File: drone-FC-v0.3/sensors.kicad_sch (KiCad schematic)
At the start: 0 parts

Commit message: what
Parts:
- added C11, C13: 0.1uF, Capacitor_SMD:C_0603_1608Metric_Pad1.08x0.95mm_HandSolder, symbol ICM-eagle-import:CAP_CERAMIC0603_NO
- added C12: 4.7uF, Capacitor_SMD:C_0603_1608Metric, symbol Device:C
- added C14, C16, C17: 0.1uF, Capacitor_SMD:C_0603_1608Metric, symbol ICM-eagle-import:CAP_CERAMIC0603_NO
- added C15: 1uF, Capacitor_SMD:C_0603_1608Metric, symbol Device:C
- added J7: ICM, Connector_PinHeader_2.54mm:PinHeader_1x06_P2.54mm_Vertical, symbol Connector:Conn_01x06_Pin
- added J8: UART0, Connector_PinHeader_2.54mm:PinHeader_1x04_P2.54mm_Vertical, symbol Connector:Conn_01x04_Pin
- added R1, R2, R3, R4: 4.7k, Resistor_SMD:R_0603_1608Metric, symbol Device:R
- added U3: LSM6DSOX, Package_LGA:LGA-14_3x2.5mm_P0.5mm_LayoutBorder3x4y, symbol Sensor_Motion:LSM6DSM
- added U4: MS5607-02BA, Package_LGA:LGA-8_3x5mm_P1.25mm, symbol Sensor_Pressure:MS5607-02BA
- added U5: LIS3MDL, Package_LGA:LGA-12_2x2mm_P0.5mm, symbol Sensor_Magnetic:LIS3MDL
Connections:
- new net: C16.1, U5.4 (C1)
- new net +3V3: C11.1, C12.1, C13.1, C14.1, C15.1, C17.1, J7.6 (Pin_6), R1.1, R2.1, R3.1, R4.1, U3.12 (CS), U3.5 (VDDIO), U3.8 (VDD), U4.1 (VDD), U4.2 (PS), U4.4 (CSB), U4.5 (CSB), U4.6 (SDO), U5.10 (~{CS}), U5.5 (Vdd), U5.6 (Vdd_IO)
- new net +5V: J8.3 (Pin_3)
- new net GND: C11.2, C12.2, C13.2, C14.2, C15.2, C16.2, C17.2, J7.4 (Pin_4), J8.4 (Pin_4), U3.1 (SDO/SA0), U3.6 (GND), U3.7 (GND), U4.3 (GND), U5.12 (GND), U5.2 (GND), U5.3 (GND), U5.9 (SDO/SA1)
- new net GPIO11: R3.2, U5.1 (SCL/SPC)
- new net GPIO12: R4.2, U5.11 (SDA/SDI/SDO)
- new net GPIO14: J7.3 (Pin_3)
- new net GPIO16: J7.2 (Pin_2)
- new net RX0: J8.2 (Pin_2)
- new net SCL: R1.2, U3.13 (SCL), U4.8 (SCLK)
- new net SDA: R2.2, U3.14 (SDA), U4.7 (SDI/SDA)
- new net TX0: J8.1 (Pin_1)
- no-connect marks 0 -> 10
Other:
- note added: "Auxiliary Ports"
- note added: "Barometer"

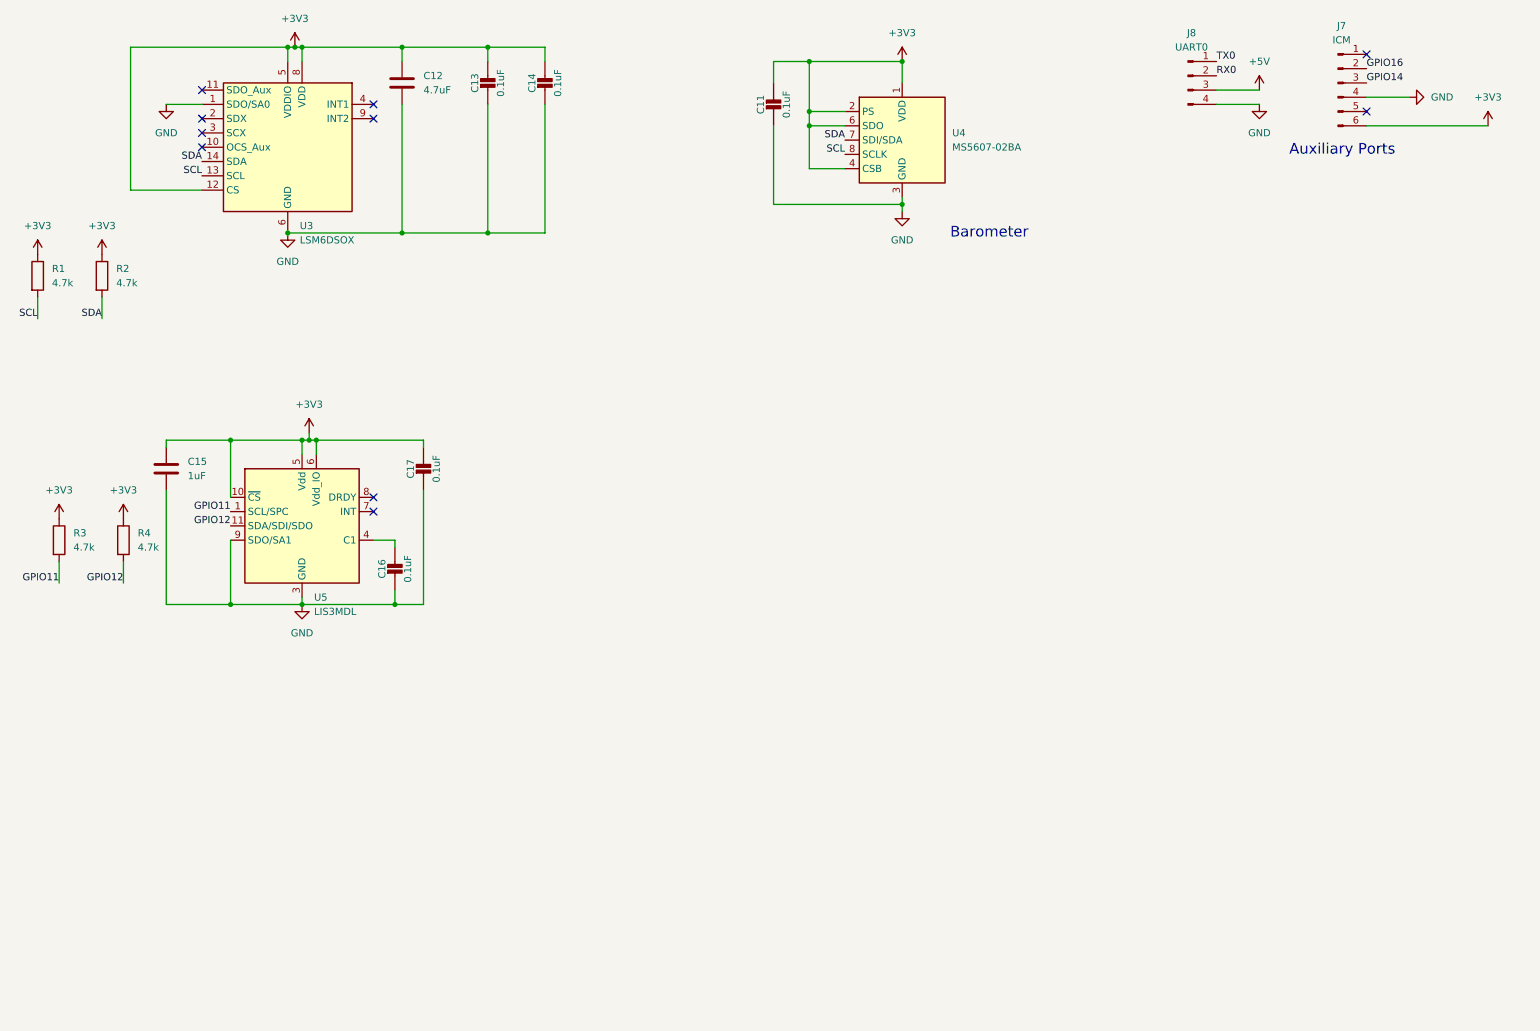
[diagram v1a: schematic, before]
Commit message: added magnetic sensor and pressure sensor
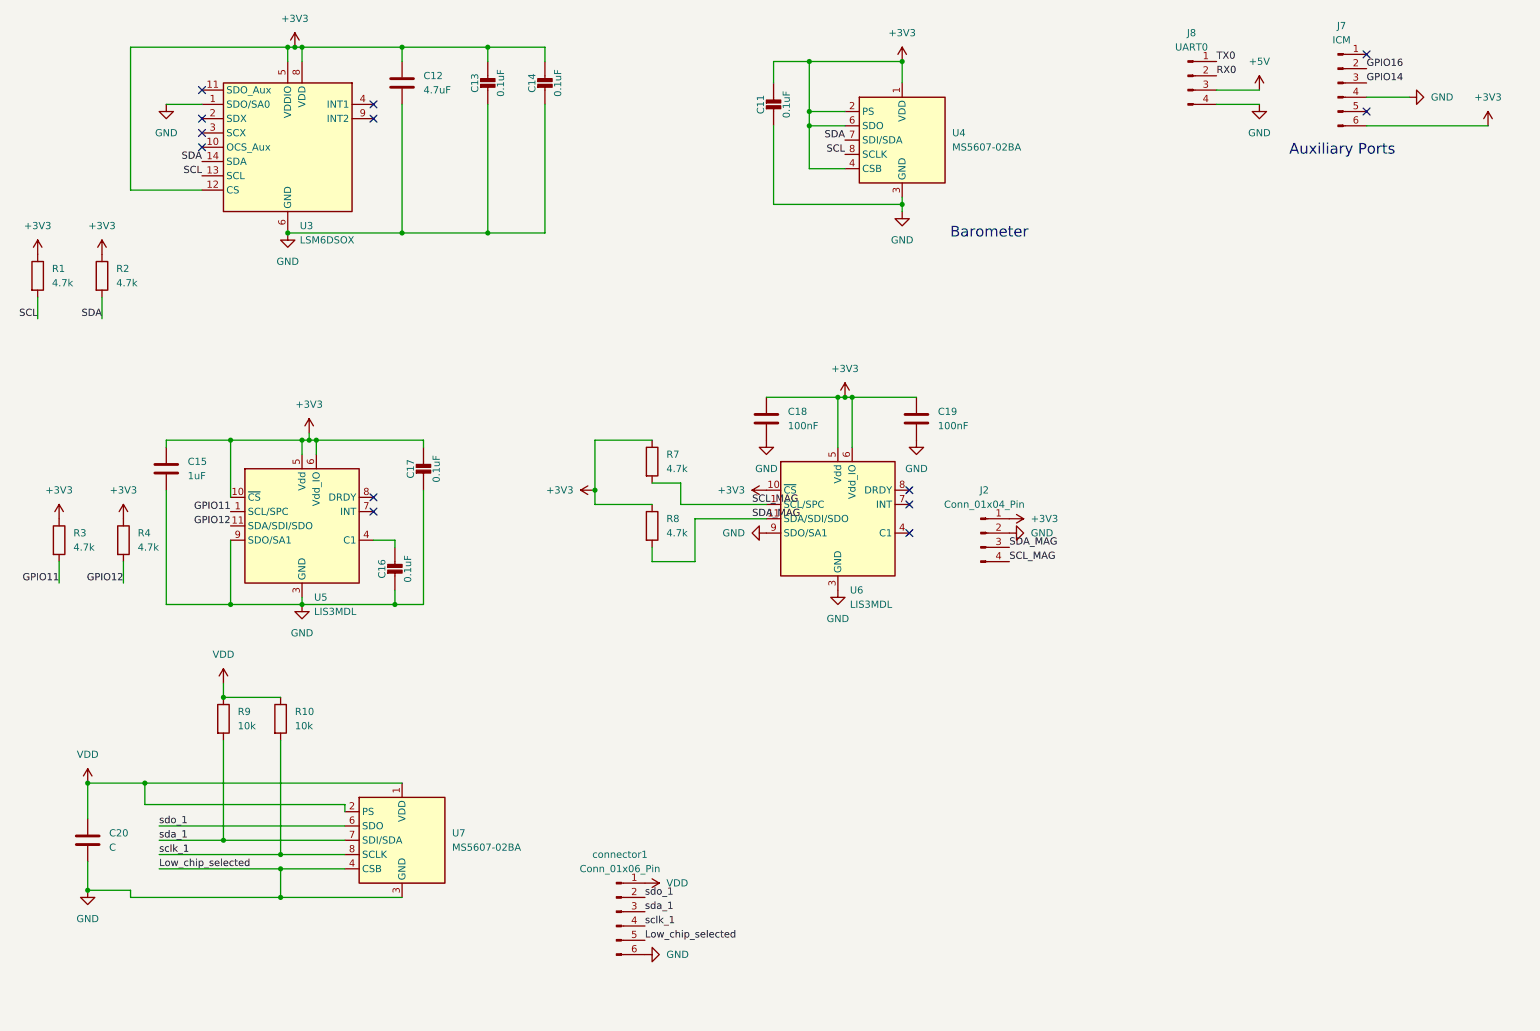
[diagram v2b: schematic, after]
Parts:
- added C18, C19: 100nF, Capacitor_SMD:C_0402_1005Metric, symbol Device:C
- added C20: C, Capacitor_SMD:C_0201_0603Metric, symbol Device:C
- added J2: Conn_01x04_Pin, Connector:FanPinHeader_1x04_P2.54mm_Vertical, symbol Connector:Conn_01x04_Pin
- added R10, R9: 10k, Resistor_SMD:R_0603_1608Metric_Pad0.98x0.95mm_HandSolder, symbol Device:R
- added R7, R8: 4.7k, Resistor_SMD:R_0402_1005Metric, symbol Device:R
- added U6: LIS3MDL, Package_LGA:LGA-12_2x2mm_P0.5mm, symbol Sensor_Magnetic:LIS3MDL
- added U7: MS5607-02BA, Package_LGA:LGA-8_3x5mm_P1.25mm, symbol Sensor_Pressure:MS5607-02BA
- added connector1: Conn_01x06_Pin, Connector_PinHeader_2.54mm:PinHeader_1x06_P2.54mm_Vertical, symbol Connector:Conn_01x06_Pin
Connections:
- net +3V3: now also C18.1, C19.1, J2.1 (Pin_1), R7.1, R8.1, U6.10 (~{CS}), U6.5 (Vdd), U6.6 (Vdd_IO)
- net GND: now also C18.2, C19.2, C20.2, J2.2 (Pin_2), U6.12 (GND), U6.2 (GND), U6.3 (GND), U6.9 (SDO/SA1), U7.3 (GND), U7.4 (CSB), U7.5 (CSB), connector1.5 (Pin_5), connector1.6 (Pin_6)
- new net SCL_MAG: J2.4 (Pin_4), R7.2, U6.1 (SCL/SPC)
- new net SDA_MAG: J2.3 (Pin_3), R8.2, U6.11 (SDA/SDI/SDO)
- new net VDD: C20.1, R10.1, R9.1, U7.1 (VDD), U7.2 (PS), connector1.1 (Pin_1)
- new net sclk_1: R10.2, U7.8 (SCLK), connector1.4 (Pin_4)
- new net sda_1: R9.2, U7.7 (SDI/SDA), connector1.3 (Pin_3)
- new net sdo_1: U7.6 (SDO), connector1.2 (Pin_2)
- no-connect marks 10 -> 13

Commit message: added USBC and IMU sensor
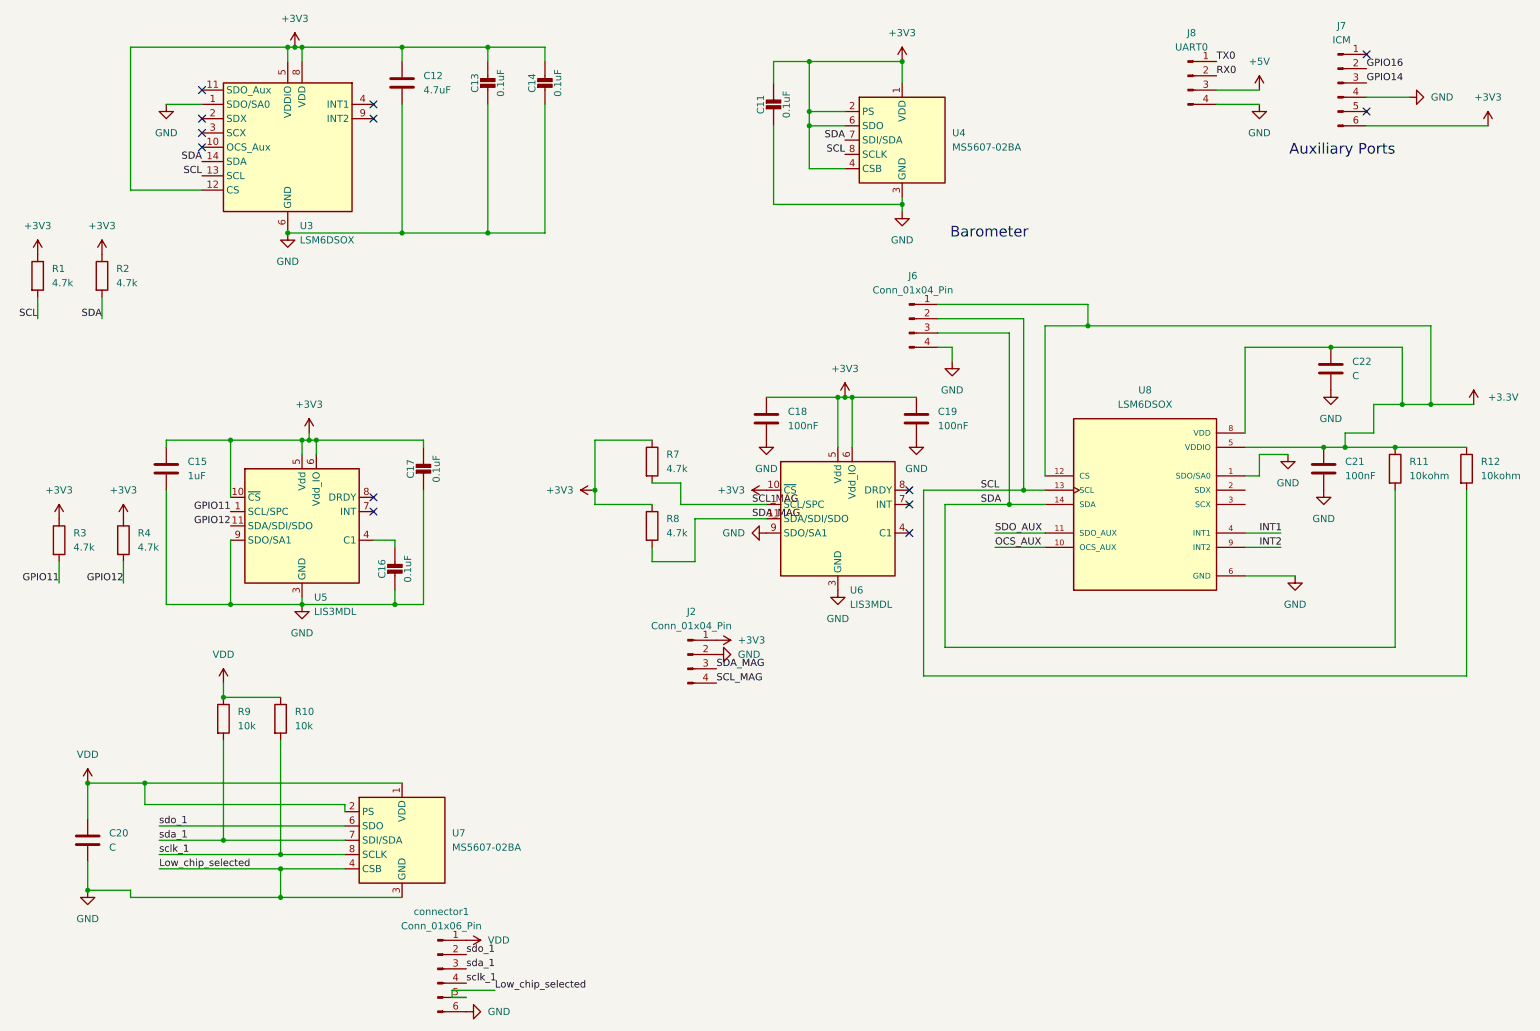
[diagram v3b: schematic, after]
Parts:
- added C21: 100nF, Capacitor_SMD:C_0603_1608Metric_Pad1.08x0.95mm_HandSolder, symbol Device:C
- added C22: C, Capacitor_SMD:C_0603_1608Metric_Pad1.08x0.95mm_HandSolder, symbol Device:C
- added J6: Conn_01x04_Pin, Connector_PinSocket_2.00mm:PinSocket_1x04_P2.00mm_Vertical, symbol Connector:Conn_01x04_Pin
- added R11, R12: 10kohm, Resistor_SMD:R_0603_1608Metric_Pad0.98x0.95mm_HandSolder, symbol Device:R
- added U8: LSM6DSOX, Package_LGA:LGA-14_3x2.5mm_P0.5mm_LayoutBorder3x4y, symbol LSM6DSOX:LSM6DSOX
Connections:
- net GND: now also C21.2, C22.2, J6.4 (Pin_4), U8.1 (SDO/SA0), U8.6 (GND), U8.7 (GND)
- net SCL: now also J6.2 (Pin_2), R12.2, U8.13 (SCL)
- net SDA: now also J6.3 (Pin_3), R11.2, U8.14 (SDA)
- new net +3.3V: C21.1, C22.1, J6.1 (Pin_1), R11.1, R12.1, U8.12 (CS), U8.5 (VDDIO), U8.8 (VDD)
- new net INT1: U8.4 (INT1)
- new net INT2: U8.9 (INT2)
- new net OCS_AUX: U8.10 (OCS_AUX)
- new net SDO_AUX: U8.11 (SDO_AUX)
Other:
- moved on the sheet: J2, connector1

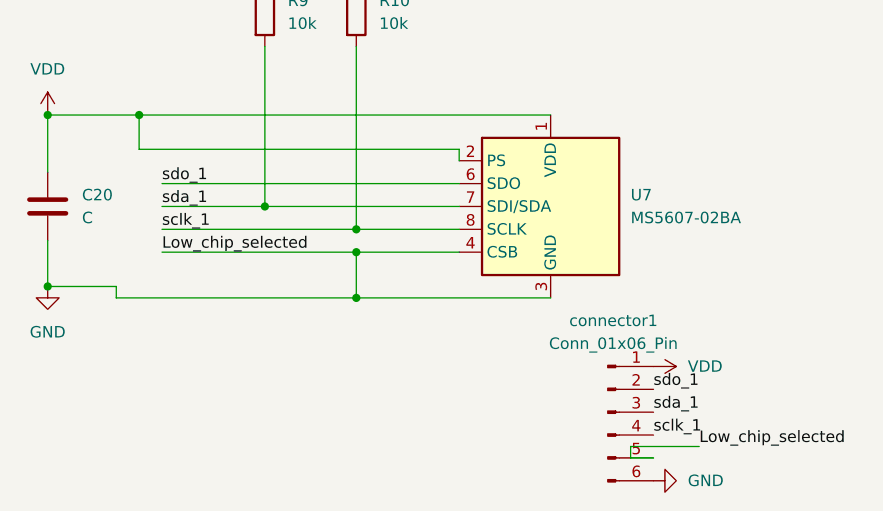
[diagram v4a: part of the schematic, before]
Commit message: added sensor connections
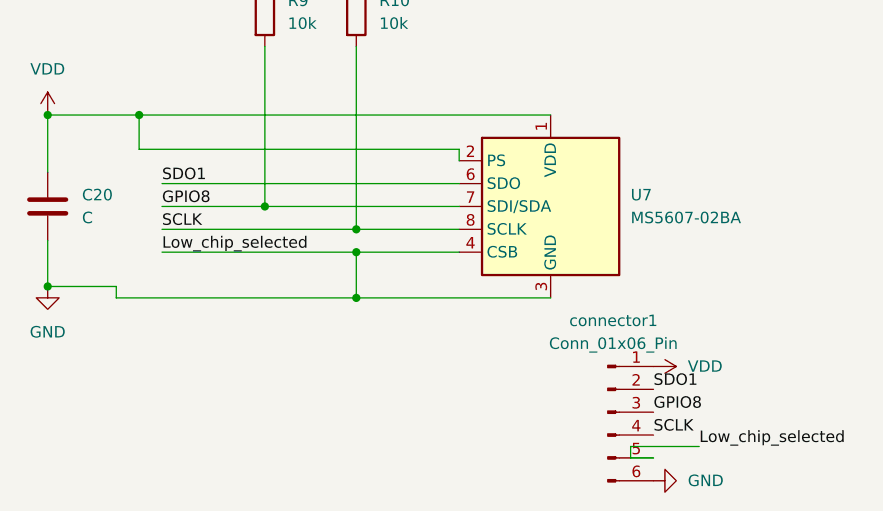
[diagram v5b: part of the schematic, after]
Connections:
- net sclk_1 renamed SCLK
- net sda_1 renamed GPIO8
- net sdo_1 renamed SDO1
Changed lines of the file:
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@@
 		)
 	)
-	(label "sda_1"
+	(label "GPIO8"
 		(at 41.91 162.56 0)
 		(effects
@@
 		)
 	)
-	(label "sdo_1"
+	(label "SDO1"
 		(at 96.52 182.88 0)
 		(effects
@@
 		)
 	)
-	(label "sdo_1"
+	(label "SDO1"
 		(at 41.91 160.02 0)
 		(effects
@@
 		)
 	)
-	(label "sclk_1"
+	(label "SCLK"
 		(at 41.91 165.1 0)
 		(effects
@@
 		)
 	)
-	(label "sda_1"
+	(label "GPIO8"
 		(at 96.52 185.42 0)
 		(effects
@@
 		)
 	)
-	(label "sclk_1"
+	(label "SCLK"
 		(at 96.52 187.96 0)
 		(effects

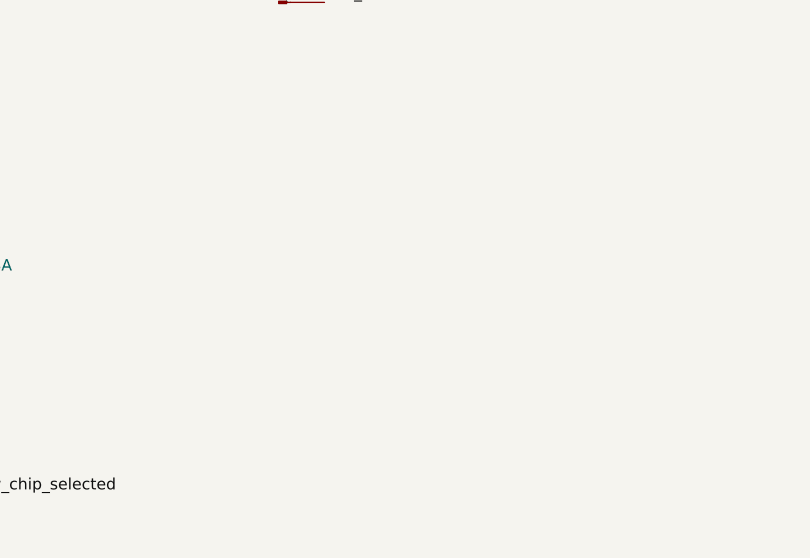
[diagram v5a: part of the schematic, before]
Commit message: added bmi088
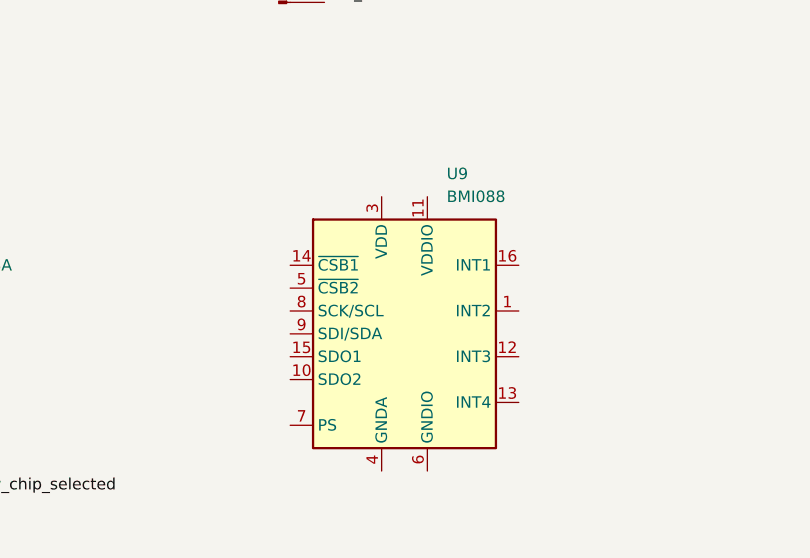
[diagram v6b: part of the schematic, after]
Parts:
- added U9: BMI088, Package_LGA:Bosch_LGA-16_4.5x3mm_P0.5mm_LayoutBorder7x1y_ClockwisePinNumbering, symbol Sensor_Motion:BMI088
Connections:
- new net: U9.2 (GNDA), U9.4 (GNDA)
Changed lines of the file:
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@@
+	)
+	(symbol
+		(lib_id "Sensor_Motion:BMI088")
+		(at 149.86 171.45 0)
+		(unit 1)
+		(body_style 1)
+		(exclude_from_sim no)
+		(in_bom yes)
+		(on_board yes)
+		(in_pos_files yes)
+		(dnp no)
+		(fields_autoplaced yes)
+		(property "Reference" "U9"
+			(at 154.5433 153.67 0)
+			(show_name no)
+			(do_not_autoplace no)
+			(effects
+				(font
+					(size 1.27 1.27)
+				)
+				(justify left)
+			)
+		)
+		(property "Value" "BMI088"
+			(at 154.5433 156.21 0)
+			(show_name no)
+			(do_not_autoplace no)
+			(effects
+				(font
+					(size 1.27 1.27)
+				)
+				(justify left)
+			)
+		)
+		(property "Footprint" "Package_LGA:Bosch_LGA-16_4.5x3mm_P0.5mm_LayoutBorder7x1y_ClockwisePinNumbering"
+			(at 133.35 172.72 0)
+			(hide yes)
+			(show_name no)
+			(do_not_autoplace no)
+			(effects
+				(font
+					(size 1.27 1.27)
+				)
+			)
+		)
+		(property "Datasheet" "https://www.bosch-sensortec.com/media/boschsensortec/downloads/datasheets/bst-bmi088-ds001.pdf"
+			(at 133.35 172.72 0)
+			(hide yes)
+			(show_name no)
+			(do_not_autoplace no)
+			(effects
+				(font
+					(size 1.27 1.27)
+				)
+			)
+		)
+		(property "Description" "Accelerometer, Gyroscope, 6-Axis Sensor, I2C / SPI interface, LGA-16"
+			(at 149.86 171.45 0)
+			(hide yes)
+			(show_name no)
+			(do_not_autoplace no)
+			(effects
+				(font
+					(size 1.27 1.27)
+				)
+			)
+		)
+		(pin "1"
+		)
+		(pin "2"
+		)
+		(pin "3"
+		)
+		(pin "4"
+		)
+		(pin "5"
+		)
+		(pin "6"
+		)
+		(pin "7"
+		)
+		(pin "10"
+		)
+		(pin "15"
+		)
+		(pin "9"
+		)
+		(pin "11"
+		)
+		(pin "13"
+		)
+		(pin "16"
+		)
+		(pin "8"
+		)
+		(pin "12"
+		)
+		(pin "14"
+		)
+		(instances
+			(project "drone-FC-v0.3"
+				(path "/3089f302-54a4-45f6-b8ae-ca1af9cfde51/c21f2c59-ba41-4889-af3a-ae43a2cc0371"
+					(reference "U9")
+					(unit 1)
+				)
+			)
+		)
 	)
 	(symbol
